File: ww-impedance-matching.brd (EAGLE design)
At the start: 135.9 x 59.4 mm, 80 parts, among them U4 ADG904BRUZ, X1 RASPI_BOARD_B+_E4P

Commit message: schematic done, basic component placement
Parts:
- removed JP_LDO_EN, JP_LDO_IN, JP_LDO_OUT: JUMPER-SMT_2_NC_PASTE_NO-SILK, Connectors:SMT-JUMPER_2_NC_PASTE_NO-SILK
- removed TP1, TP2, TP3: TPTP14R, TestPoints:TP14R
- removed U4: ADG904BRUZ, Switches:SOP65P640X120-20N
- added C13: 1u, Capacitors:C0603
- added C14: (no value), Capacitors:C0805
- added JP.LDO.EN, JP.LDO.IN, JP.LDO.OUT: JUMPER-SMT_2_NC_PASTE_NO-SILK, Connectors:SMT-JUMPER_2_NC_PASTE_NO-SILK
- added MUX.RF.OUT: ADG904BRUZ, Switches:SOP65P640X120-20N
- R_SCL, R_SDA: value (none) -> 10k
- moved C10 200.6 mm to (113.2, -44.3)
- moved C8 200.5 mm to (111.0, -34.8), turned to 90 degrees
- moved C6 183.6 mm to (89.3, -34.8), turned to 270 degrees
- moved C2 183.1 mm to (91.4, -44.5)
- moved C9 168.6 mm to (46.1, 20.8), turned to 180 degrees
- moved C12 168.1 mm to (17.0, 37.0), turned to 180 degrees
- moved C11 158.8 mm to (5.59, 37.1), turned to 180 degrees
- moved C4 151.0 mm to (65.3, -34.8), turned to 90 degrees
- moved C7 124.8 mm to (-47.1, 30.0)
- moved C3 124.1 mm to (41.9, -45.7), turned to 180 degrees
- moved C1 124.1 mm to (39.8, -35.8), turned to 90 degrees
- moved U_LDO2.7 110.5 mm to (-1.27, 45.7)
- moved MUX.RF.IN 108.6 mm to (49.5, 25.4), turned to 90 degrees
- moved JP_SDA 103.4 mm to (16.5, 48.3), turned to 90 degrees
- moved JP_SCL 99.9 mm to (19.1, 48.3), turned to 270 degrees
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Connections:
- net N$1 renamed 5V.JMP
- net N$2 renamed 3V3.JMP
- net N$3 renamed SDA.IN
- net N$5 renamed SCL.IN
- removed net N$13: TP1.TP, X1.7
- removed net N$14: TP2.TP, X1.22
- removed net N$16: TP3.TP, X1.18
- removed net N$7: JP_LDO_IN.1, U_LDO2.7.1
- removed net N$8: JP_LDO_OUT.2, U_LDO2.7.5
- removed net VIN: C11.1, C12.1, C7.1, C9.1, MUX.RF.IN.2, MUX.SCL.2, MUX.SDA.2, U4.2
- new net LDO.IN: C13.1, JP.LDO.IN.1, U_LDO2.7.1
- new net LDO.OUT: JP.LDO.OUT.2, U_LDO2.7.5
- net +5V: now also JP.LDO.EN.2, JP.LDO.IN.2; no longer JP_LDO_EN.2, JP_LDO_IN.2
- net 2.7V: now also C11.1, C12.1, C14.1, C7.1, C9.1, JP.LDO.OUT.1, MUX.RF.IN.2, MUX.RF.OUT.2, MUX.SCL.2, MUX.SDA.2; no longer JP_LDO_OUT.1
- net F0.OUT: now also MUX.RF.OUT.4; no longer U4.4
- net F1.OUT: now also MUX.RF.OUT.17; no longer U4.17
- net F2.OUT: now also MUX.RF.OUT.7; no longer U4.7
- net F3.OUT: now also MUX.RF.OUT.14; no longer U4.14
- net GND: now also C13.2, C14.2, MUX.RF.OUT.1, MUX.RF.OUT.11, MUX.RF.OUT.12, MUX.RF.OUT.13, MUX.RF.OUT.15, MUX.RF.OUT.16, MUX.RF.OUT.18, MUX.RF.OUT.3, MUX.RF.OUT.5, MUX.RF.OUT.6, MUX.RF.OUT.8, MUX.RF.OUT.9; no longer U4.1, U4.11, U4.12, U4.13, U4.15, U4.16, U4.18, U4.3, U4.5, U4.6, U4.8, U4.9
- net MUX.A0: now also MUX.RF.OUT.20; no longer U4.20
- net MUX.A1: now also MUX.RF.OUT.19; no longer U4.19
- net N$9: now also JP.LDO.EN.1; no longer JP_LDO_EN.1
- net RF_OUT: now also MUX.RF.OUT.10; no longer U4.10
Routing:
- added copper zone on layer 1, net GND
- added copper zone on layer 16, net GND

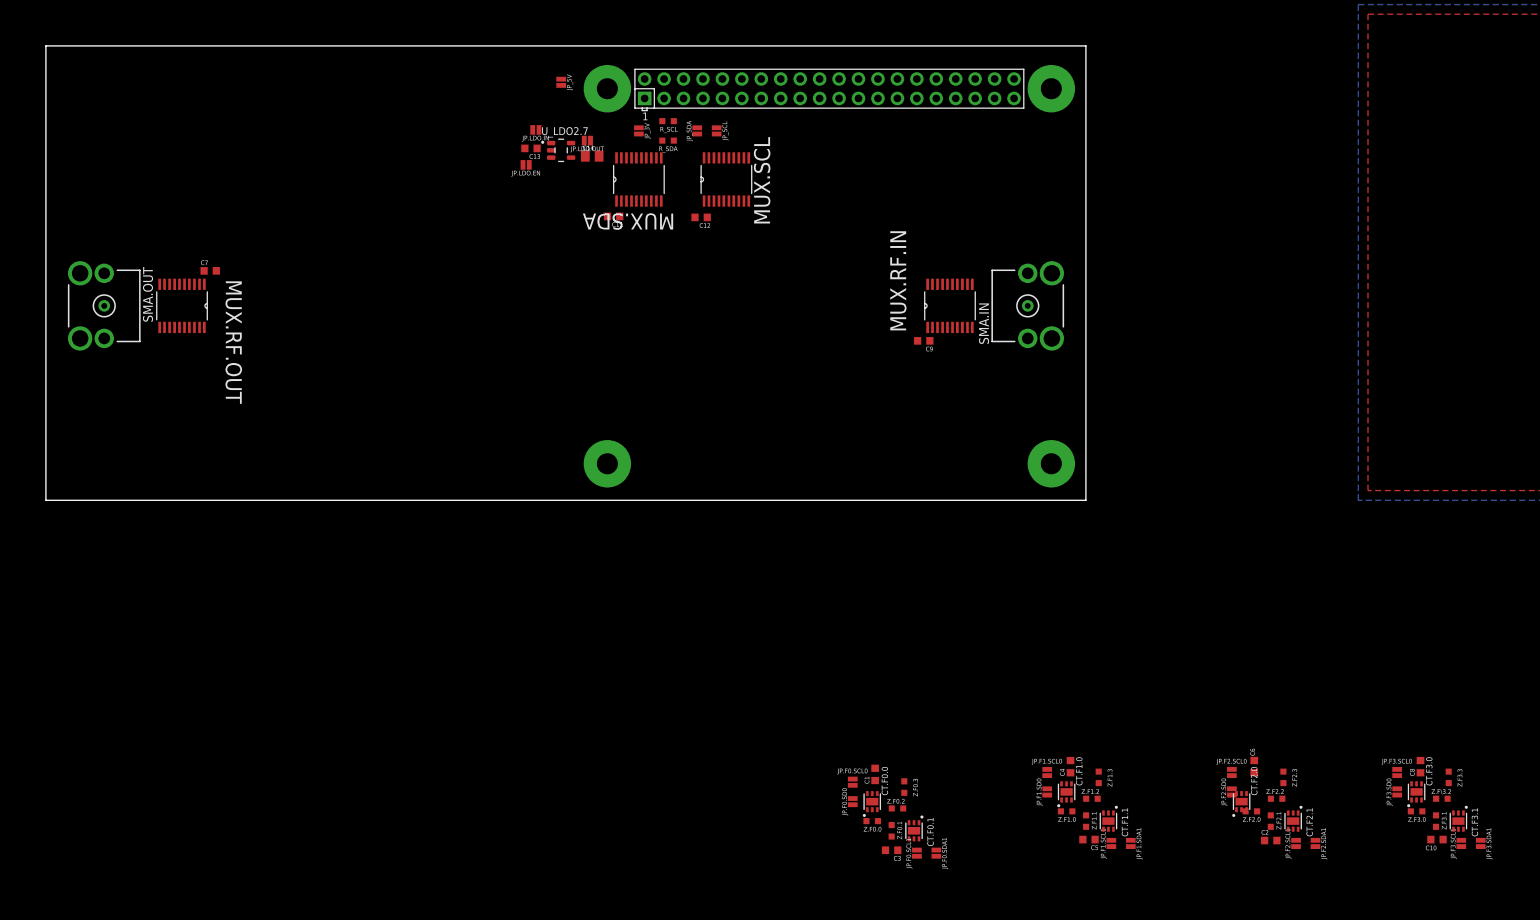
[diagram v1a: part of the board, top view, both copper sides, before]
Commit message: filter placement
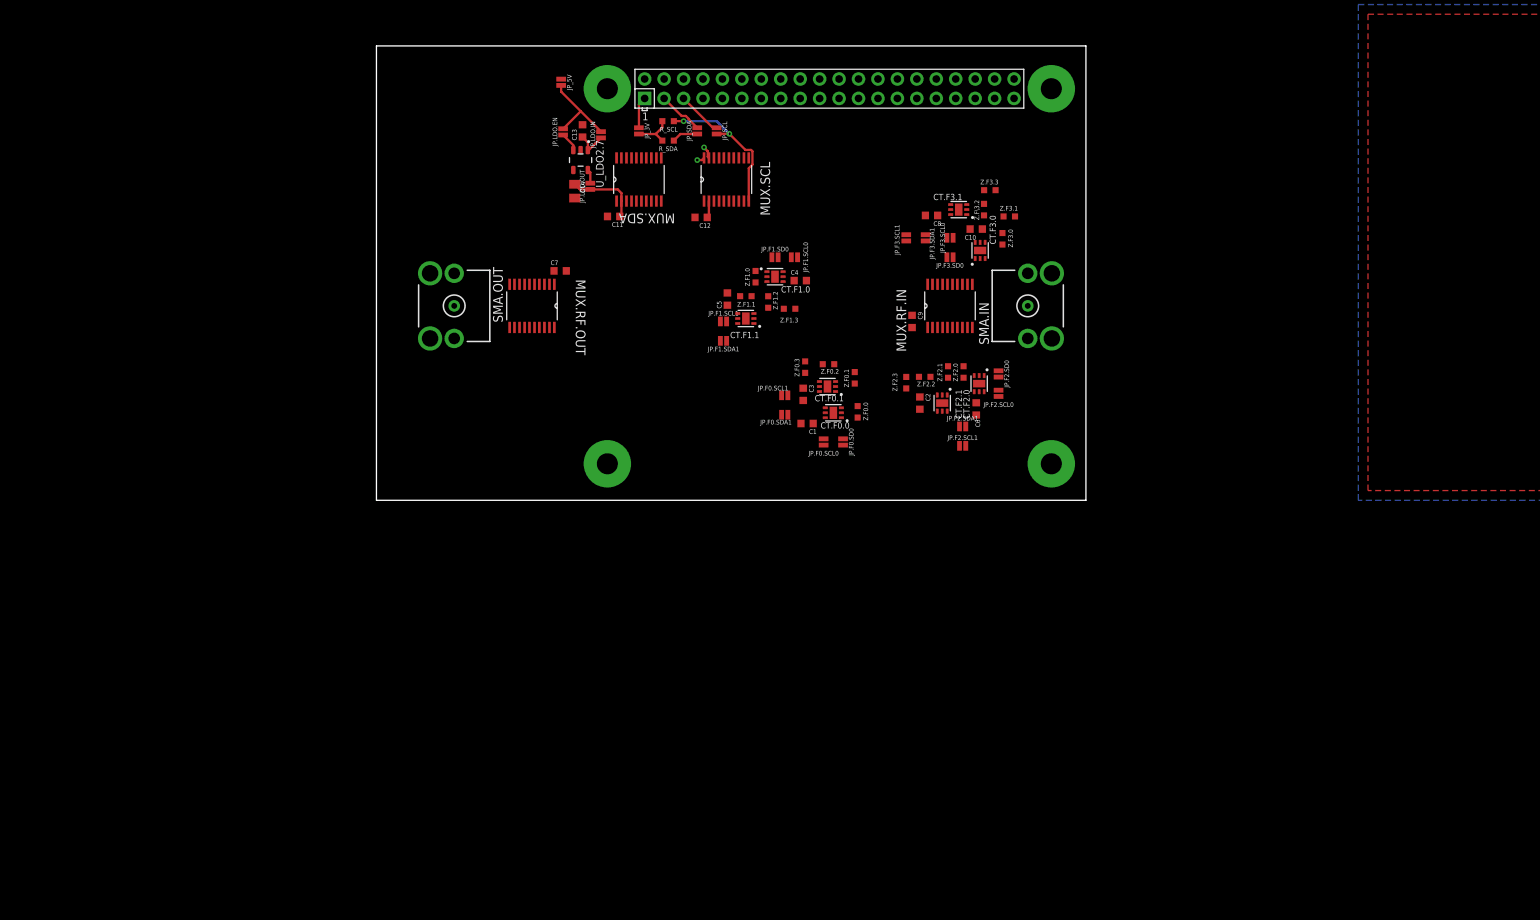
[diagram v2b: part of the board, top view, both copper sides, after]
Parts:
- moved JP.F3.SCL1 107.3 mm to (43.8, 34.3)
- moved JP.F3.SDA1 107.3 mm to (46.4, 34.3)
- moved CT.F3.1 103.2 mm to (50.7, 38.0), turned to 180 degrees
- moved C10 99.9 mm to (53.0, 35.4)
- moved Z.F\3.2 97.5 mm to (54.0, 38.0), turned to 270 degrees
- moved Z.F3.3 97.4 mm to (54.7, 40.5), turned to 0 degrees
- moved Z.F3.1 96.7 mm to (57.3, 37.1), turned to 0 degrees
- moved C8 96.3 mm to (47.1, 37.2), turned to 180 degrees
- moved Z.F3.0 92.3 mm to (56.4, 34.2), turned to 270 degrees
- moved JP.F3.SCL0 91.1 mm to (49.5, 34.3), turned to 0 degrees
- moved JP.F3.SD0 91.1 mm to (49.5, 31.8), turned to 0 degrees
- moved CT.F3.0 90.9 mm to (53.5, 32.6)
- moved JP.F1.SCL1 85.0 mm to (19.9, 23.4), turned to 0 degrees
- moved C5 85.0 mm to (20.4, 26.3), turned to 90 degrees
- moved JP.F1.SDA1 84.5 mm to (19.9, 20.8), turned to 180 degrees
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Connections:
- net N$29 renamed RF.F1.0
- net N$39 renamed RF.F3.0
- net N$4 renamed RF.F0.0
- net N$49 renamed RF.F2.0
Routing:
- net SCL: track 0.00 -> 20.3 mm, vias 0 -> 2
- net 2.7V: track 0.00 -> 11.9 mm
- net +5V: track 0.00 -> 11.5 mm
- net SDA.IN: track 0.00 -> 5.95 mm
- net SCL.IN: track 0.00 -> 5.92 mm
- net +3V3: track 0.00 -> 5.45 mm
- net LDO.IN: track 0.00 -> 4.38 mm
- net 3V3.JMP: track 0.00 -> 4.14 mm
- net SDA: track 0.00 -> 3.42 mm
- net N$9: track 0.00 -> 2.53 mm
- net LDO.OUT: track 0.00 -> 1.86 mm
- net MUX.A1: track 0.00 -> 1.63 mm, vias 0 -> 1
- net MUX.A0: track 0.00 -> 1.00 mm, vias 0 -> 1
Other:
- board size 135.9 x 59.4 mm -> 92.7 x 59.4 mm

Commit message: mostly routed
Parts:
- removed JP.F0.SD0, JP.F1.SD0, JP.F2.SD0, JP.F3.SD0: JUMPER-SMT_2_NC_PASTE_NO-SILK, Connectors:SMT-JUMPER_2_NC_PASTE_NO-SILK
- added JP.F0.SDA0, JP.F1.SDA0, JP.F2.SDA0, JP.F3.SDA0: JUMPER-SMT_2_NC_PASTE_NO-SILK, Connectors:SMT-JUMPER_2_NC_PASTE_NO-SILK
- moved T.M1 248.0 mm to (42.9, 47.0)
- moved T.M0 237.0 mm to (29.1, 47.5)
- moved R2 223.4 mm to (39.5, 49.5), turned to 180 degrees
- moved R3 218.8 mm to (33.0, 44.5), turned to 90 degrees
- moved MUX0 217.0 mm to (33.0, 48.3), turned to 180 degrees
- moved MUX1 215.9 mm to (36.1, 48.3), turned to 180 degrees
- moved R1 211.0 mm to (29.2, 49.5)
- moved R4 210.3 mm to (36.1, 44.5), turned to 90 degrees
- moved MUX.RF.OUT 24.8 mm to (19.7, 24.4), turned to 90 degrees
- moved SMA.OUT 24.2 mm to (8.89, 24.1)
- moved C7 20.5 mm to (16.4, 19.8), turned to 180 degrees
- moved Z.F1.1 18.5 mm to (40.4, 32.5), turned to 0 degrees
- moved CT.F1.1 15.9 mm to (36.6, 31.9)
- moved Z.F1.0 15.5 mm to (39.6, 29.2), turned to 270 degrees
- moved Z.F1.2 14.1 mm to (36.7, 34.8), turned to 0 degrees
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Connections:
- net F0.SDA: now also JP.F0.SDA0.1; no longer JP.F0.SD0.1
- net F0SDA0: now also JP.F0.SDA0.2; no longer JP.F0.SD0.2
- net F1.SDA: now also JP.F1.SDA0.1; no longer JP.F1.SD0.1
- net F1SDA0: now also JP.F1.SDA0.2; no longer JP.F1.SD0.2
- net F2.SDA: now also JP.F2.SDA0.1; no longer JP.F2.SD0.1
- net F2SDA0: now also JP.F2.SDA0.2; no longer JP.F2.SD0.2
- net F3.SDA: now also JP.F3.SDA0.1; no longer JP.F3.SD0.1
- net F3SDA0: now also JP.F3.SDA0.2; no longer JP.F3.SD0.2
- net N$11: now also X1.13; no longer X1.12
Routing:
- net MUX.A0: track 1.00 -> 122.3 mm, vias 1 -> 4
- net MUX.A1: track 1.63 -> 121.5 mm, vias 1 -> 2
- net 2.7V: track 11.9 -> 102.0 mm, vias 0 -> 4
- net F2.SDA: track 0.00 -> 83.8 mm, vias 0 -> 3
- net F0.SDA: track 0.00 -> 73.3 mm, vias 0 -> 2
- net F2.SCL: track 0.00 -> 69.6 mm, vias 0 -> 2
- net F3.SDA: track 0.00 -> 50.2 mm, vias 0 -> 2
- net F1.SDA: track 0.00 -> 44.1 mm, vias 0 -> 3
- net F3.OUT: track 0.00 -> 43.6 mm
- net F0.SCL: track 0.00 -> 41.8 mm, vias 0 -> 3
- net F3.SCL: track 0.00 -> 36.1 mm, vias 0 -> 4
- net GND: track 0.00 -> 34.6 mm
- net F2.OUT: track 0.00 -> 30.1 mm, vias 0 -> 2
- net +3V3: track 5.45 -> 35.0 mm, vias 0 -> 3
- net F1.SCL: track 0.00 -> 28.3 mm, vias 0 -> 2
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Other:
- board size 92.7 x 59.4 mm -> 69.8 x 59.4 mm

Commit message: routed and passed DRC
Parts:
- moved C14 0.25 mm to (5.08, 39.6)
- moved JP.F1.SCL0 0.25 mm to (35.6, 25.1)
- moved JP.F1.SDA0 0.25 mm to (38.1, 25.1)
- moved JP.F2.SCL0 0.13 mm to (58.5, 14.0)
- moved JP.F2.SDA0 0.13 mm to (58.5, 16.5)
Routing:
- net +3V3: track 35.0 -> 210.1 mm, vias 3 -> 9
- net SCL: track 9.60 -> 25.7 mm
- net MUX.A1: track 121.5 -> 108.7 mm
- net MUX.A0: track 122.3 -> 109.7 mm
- net SDA: track 3.42 -> 14.6 mm, vias 0 -> 2
- net GND: track 34.6 -> 37.7 mm, vias 0 -> 309
- net +5V: track 9.97 -> 9.00 mm
- net F1.SDA: track 44.1 -> 45.0 mm

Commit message: ready to submit rev A for production
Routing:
- net GND: track 37.7 -> 19.2 mm

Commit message: revA production
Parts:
- added LOGO1: LOGO-CMU, Graphics:CMU_LOGO
- moved JP.F0.SCL1 0.90 mm to (31.1, 14.4)
- moved JP.F0.SDA1 0.81 mm to (31.0, 11.8)
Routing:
- net F0.SDA: track 73.3 -> 74.4 mm
- net F0.SCL: track 41.8 -> 42.8 mm
- net F0SDA1: track 7.49 -> 6.72 mm
- net F0SCL1: track 4.33 -> 3.77 mm
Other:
- board text added: "Filter 0"
- board text added: "Filter 1"
- board text added: "Filter 2"
- board text added: "Filter 3"
- board text added: "Wired Wireless Z-Matcher rev A Reese Grimsley"
